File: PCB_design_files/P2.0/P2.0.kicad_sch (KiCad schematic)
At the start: 54 parts, among them J1 EEG_IN, J3 SWD, U1 INA819IDRGR, U3 TPS61094, U4 TPS60400, U5 NRF52832-QFAA-R, X1 32MHz

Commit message: P2.0
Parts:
- C1, C10, C11, C2, C7: footprint Capacitor_SMD:C_0805_2012Metric -> Capacitor_SMD:C_0402_1005Metric; Purchasing (none) -> https://www.digikey.ca/en/products/detail/murata-electronic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
- C12, C13, C14, C15, C16, C17, C18, L1: Purchasing (none) -> https://www.digikey.ca/en/products/detail/murata-electronic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
- C19, C20: footprint Capacitor_SMD:C_0603_1608Metric -> Capacitor_SMD:C_0402_1005Metric; Purchasing (none) -> https://www.digikey.ca/en/products/detail/murata-electronic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
- C3, C4, C5, C6: footprint Capacitor_SMD:C_0201_0603Metric -> Capacitor_SMD:C_0402_1005Metric; Purchasing (none) -> https://www.digikey.ca/en/products/detail/murata-electronic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
- C8: Field4 (none) -> https://www.digikey.ca/en/products/detail/murata-electronic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
- C9: Purchasing (none) -> https://www.digikey.ca/en/products/detail/tdk-corporation/C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
- L2, L3: footprint Inductor_SMD:L_0402_1005Metric -> Inductor_SMD:L_Murata_DFE201610P; Purchasing (none) -> https://www.digikey.ca/en/products/detail/murata-electronic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
- R1, R2: footprint Resistor_SMD:R_0402_1005Metric -> Resistor_SMD:R_0805_2012Metric; Purchasing (none) -> https://www.digikey.ca/en/products/detail/panasonic-electro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
- R10, R11, R12, R13, R14, R16, R17, R18, R19, R20, R4, R5, R7, R8, R9: footprint Resistor_SMD:R_0402_1005Metric -> Resistor_SMD:R_0805_2012Metric; Purchasing (none) -> https://www.digikey.ca/en/products/detail/stackpole-electro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
- R3: footprint Resistor_SMD:R_0402_1005Metric -> Resistor_SMD:R_0805_2012Metric; Puchasing (none) -> https://www.digikey.ca/en/products/detail/stackpole-electro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
- R6: value 100k -> 20k; footprint Resistor_SMD:R_0402_1005Metric -> Resistor_SMD:R_0805_2012Metric; Purchasing (none) -> https://www.digikey.ca/en/products/detail/stackpole-electro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
- U1: footprint Library:SON_9IDRGR_TEX -> Package_SON:WSON-8-1EP_3x3mm_P0.5mm_EP1.45x2.4mm_ThermalVias; Purchasing (none) -> https://www.digikey.ca/en/products/detail/texas-instruments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
- U2: footprint (none) -> Package_DFN_QFN:Texas_R-PUQFN-N10; Purchasing (none) -> https://www.digikey.com/en/products/detail/texas-instrument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
- U3: footprint Library:TPS61094DSSR -> Package_SON:WSON-12-1EP_3x2mm_P0.5mm_EP1x2.65_ThermalVias; Purchasing (none) -> https://www.digikey.ca/en/products/detail/texas-instruments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
- U4: footprint (none) -> Package_TO_SOT_SMD:SOT-23-5; Puchasing (none) -> https://www.digikey.com/en/products/detail/texas-instrument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
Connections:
- net +3V3: now also U4.2 (IN); no longer U4.1 (IN)
- net -3V3: now also U4.1 (OUT); no longer U4.5 (OUT)
- net GND: now also U4.4 (GND); no longer U4.2 (GND)
- net at C10.1: now also U4.5 (CFLY+); no longer U4.3 (CFLY+)
- net at C10.2: now also U4.3 (CFLY-); no longer U4.4 (CFLY-)
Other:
- moved on the sheet: C10

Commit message: Updated schematic
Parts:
- removed J3: SWD, symbol Connector:Conn_01x03_Pin
- removed X1: 32MHz, symbol Device:Crystal
- added J2: 20021121-00008C4LF, 20021121_00008C4LF:AMPHENOL_20021121-00008C4LF, symbol Connector_Generic:Conn_02x04_Counter_Clockwise
- added Y1: 32MHz, ECS_320_8_37CKM:XTAL_ECS-320-8-37CKM, symbol Device:Crystal_GND24
- AE1: Purchasing (none) -> https://www.digikey.ca/en/products/detail/johanson-technolo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
- BT1: footprint Connector_JST:JST_ACH_BM02B-ACHSS-GAN-ETF_1x02-1MP_P1.20mm_Vertical -> Connector_PinSocket_2.54mm:PinSocket_1x02_P2.54mm_Vertical; Purchasing (none) -> n/a
- J1: footprint Connector_JST:JST_SH_BM02B-SRSS-TB_1x02-1MP_P1.00mm_Vertical -> Connector_PinSocket_2.54mm:PinSocket_1x02_P2.54mm_Vertical; Purchasing (none) -> n/a
- U2: value ~ -> TLV9102
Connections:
- net +3V3: now also J2.2 (Pin_2)
- net GND: now also J2.3 (Pin_3), J2.4 (Pin_4), Y1.2, Y1.4
- net STAGE_3_OUT: now also J2.1 (Pin_1)
- net at C18.2, U5.34 (XC1): now also Y1.3
- net SWO: now reaches U5.21 (P0.18/TRACEDATA[0]/SWO)
- net SWO: now also J2.6 (Pin_6)
- net NRST: now reaches U5.24 (P0.21/Nreset)
- net NRST: now also J2.5 (Pin_5)
- net SWDCLK: now reaches U5.25 (SWDCLK)
- net SWDCLK: now also J2.7 (Pin_7)
- net SWDIO: now reaches U5.26 (SWDIO)
- net SWDIO: now also J2.8 (Pin_8)
- net at C16.2, U5.35 (XC2): now also Y1.1
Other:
- note added: "4. Debug Header"
- moved on the sheet: C13, C16, C17, C18, C21

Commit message: Updated LED footprint
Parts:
- D1: footprint LED_SMD:LED_0402_1005Metric -> LED_SMD:LED_0603_1608Metric; Purchasing (none) -> https://www.digikey.ca/en/products/detail/w%C3%BCrth-elektr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
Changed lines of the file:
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@@
       (effects (font (size 1.27 1.27)) (justify right))
     )
-    (property "Footprint" "LED_SMD:LED_0402_1005Metric" (at 199.39 143.51 0)
+    (property "Footprint" "LED_SMD:LED_0603_1608Metric" (at 199.39 143.51 0)
       (effects (font (size 1.27 1.27)) hide)
     )
-    (property "Datasheet" "~" (at 199.39 143.51 0)
+    (property "Datasheet" "https://www.we-online.com/components/products/datasheet/150060VS75000.pdf" (at 199.39 143.51 0)
       (effects (font (size 1.27 1.27)) hide)
     )
+    (property "Purchasing" "https://www.digikey.ca/en/products/detail/w%C3%BCrth-elektronik/150060VS75000/4489906" (at 199.39 143.51 90)
+      (effects (font (size 1.27 1.27)) hide)
+    )

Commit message: Added decoupling capacitors and updated layout
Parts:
- added C22, C23, C24, C25: .1uF, Capacitor_SMD:C_0402_1005Metric, symbol Device:C
- C21: value N.C. -> ~; now fitted; now left out of the parts list
- J1: footprint Connector_PinSocket_2.54mm:PinSocket_1x02_P2.54mm_Vertical -> Connector_PinHeader_2.54mm:PinHeader_1x02_P2.54mm_Vertical
- R18, R20: footprint Resistor_SMD:R_0805_2012Metric -> Resistor_SMD:R_0603_1608Metric; Purchasing https://www.digikey.ca/en/products/detail/stackpole-electro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 -> (none)
- U1: footprint Package_SON:WSON-8-1EP_3x3mm_P0.5mm_EP1.45x2.4mm_ThermalVias -> Package_SON:WSON-8-1EP_3x3mm_P0.5mm_EP1.45x2.4mm
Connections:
- net +3V3: now also C22.2, C24.1
- net -3V3: now also C23.2, C25.2
- net GND: now also C22.1, C23.1, C24.2, C25.1
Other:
- moved on the sheet: C2, C3, C4, C5, C6, C7, R10, R11, R12, R13, R14, R16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

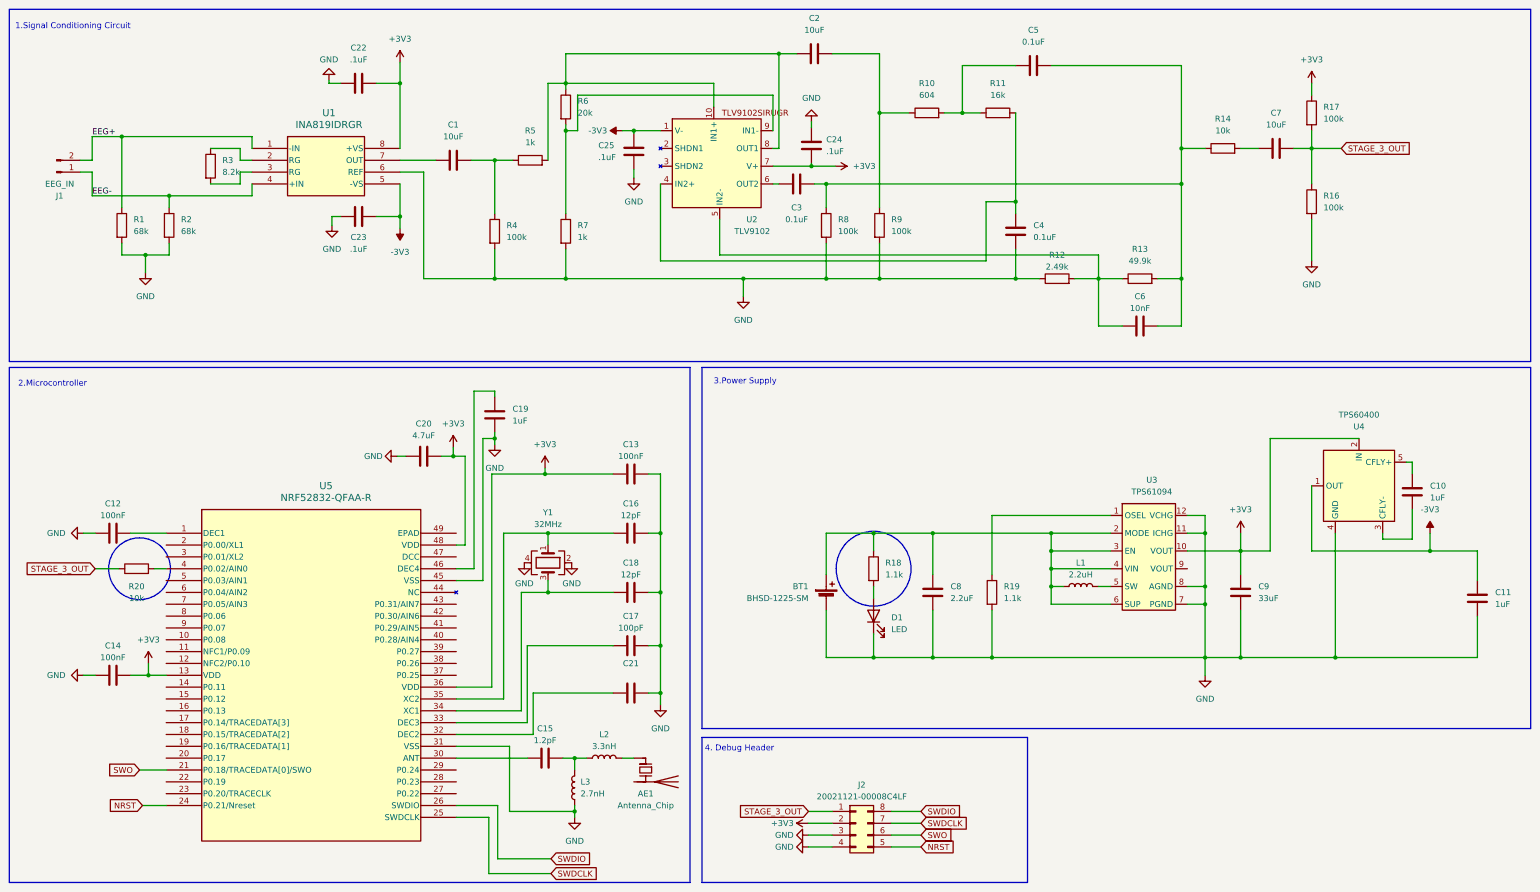
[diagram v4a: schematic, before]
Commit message: PCB layout updates
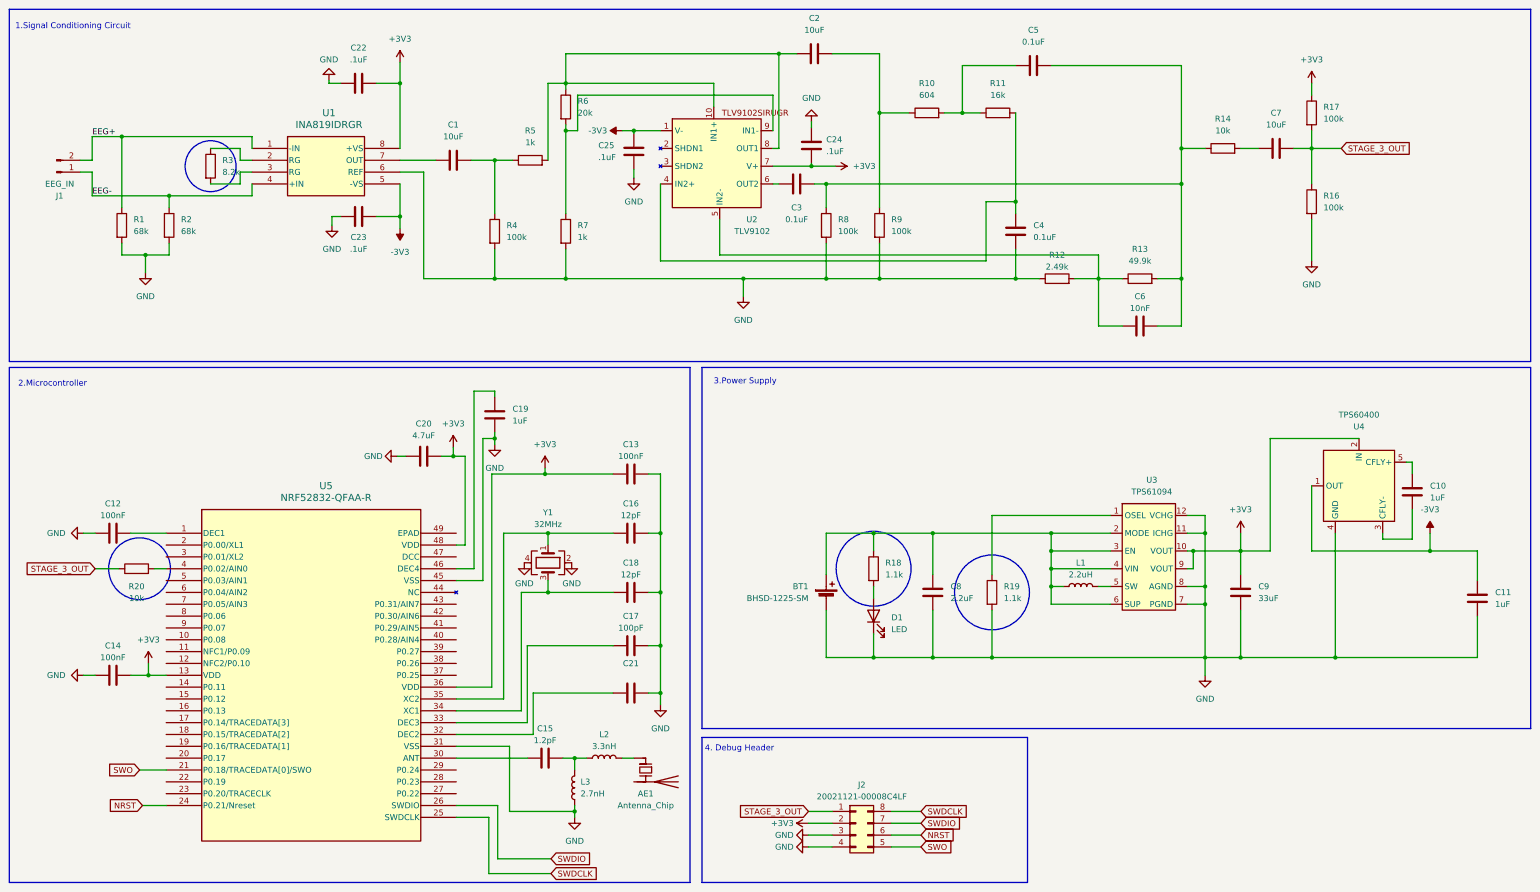
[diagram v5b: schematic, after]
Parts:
- R19: footprint Resistor_SMD:R_0805_2012Metric -> Resistor_SMD:R_0603_1608Metric; Purchasing https://www.digikey.ca/en/products/detail/stackpole-electro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 -> (none)
- R3: footprint Resistor_SMD:R_0805_2012Metric -> Resistor_SMD:R_0603_1608Metric
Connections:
- net +3V3: now also U3.9 (VOUT)
- net NRST: now also J2.6 (Pin_6); no longer J2.5 (Pin_5)
- net SWDCLK: now also J2.8 (Pin_8); no longer J2.7 (Pin_7)
- net SWDIO: now also J2.7 (Pin_7); no longer J2.8 (Pin_8)
- net SWO: now also J2.5 (Pin_5); no longer J2.6 (Pin_6)
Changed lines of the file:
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@@
   (junction (at 118.11 45.72) (diameter 0) (color 0 0 0 0)
   )
+  (junction (at 267.97 129.54) (diameter 0) (color 0 0 0 0)
+  )
   (junction (at 278.13 129.54) (diameter 0) (color 0 0 0 0)
   )
@@
   (junction (at 153.67 149.86) (diameter 0) (color 0 0 0 0)
   )
+  (wire (pts (xy 267.97 129.54) (xy 278.13 129.54))
+    (stroke (width 0) (type default))
+  )
   (wire (pts (xy 102.87 48.26) (xy 102.87 71.12))
     (stroke (width 0) (type default))
@@
     (stroke (width 0) (type default))
   )
+  (wire (pts (xy 266.7 133.35) (xy 267.97 133.35))
+    (stroke (width 0) (type default))
+  )
   (wire (pts (xy 189.23 50.8) (xy 265.43 50.8))
     (stroke (width 0) (type default))
@@
     (stroke (width 0) (type default))
   )
+  (wire (pts (xy 267.97 133.35) (xy 267.97 129.54))
+    (stroke (width 0) (type default))
+  )
   (wire (pts (xy 118.11 64.77) (xy 118.11 71.12))
     (stroke (width 0) (type default))
@@
     (stroke (width 0) (type default))
   )
-  (wire (pts (xy 266.7 129.54) (xy 278.13 129.54))
+  (wire (pts (xy 266.7 129.54) (xy 267.97 129.54))
     (stroke (width 0) (type default))
   )
@@
     (fill (type none))
   )
+  (circle (center 224.79 138.43) (radius 8.0322)
+    (stroke (width 0) (type default))
+    (fill (type none))
+  )
   (rectangle (start 162.56 90.17) (end 340.36 167.64)
+    (stroke (width 0) (type default))
+    (fill (type none))
+  )
+  (circle (center 57.15 46.99) (radius 5.4625)
     (stroke (width 0) (type default))
     (fill (type none))
@@
     )
   )
-  (global_label "NRST" (shape input) (at 209.55 193.04 0) (fields_autoplaced)
+  (global_label "SWO" (shape input) (at 209.55 193.04 0) (fields_autoplaced)
     (effects (font (size 1.27 1.27)) (justify left))
-    (property "Intersheetrefs" "${INTERSHEET_REFS}" (at 217.3128 193.04 0)
+    (property "Intersheetrefs" "${INTERSHEET_REFS}" (at 216.5266 193.04 0)
       (effects (font (size 1.27 1.27)) (justify left) hide)
     )
@@
     )
   )
-  (global_label "SWO" (shape input) (at 209.55 190.5 0) (fields_autoplaced)
+  (global_label "NRST" (shape input) (at 209.55 190.5 0) (fields_autoplaced)
     (effects (font (size 1.27 1.27)) (justify left))
-    (property "Intersheetrefs" "${INTERSHEET_REFS}" (at 216.5266 190.5 0)
+    (property "Intersheetrefs" "${INTERSHEET_REFS}" (at 217.3128 190.5 0)
       (effects (font (size 1.27 1.27)) (justify left) hide)
     )
@@
     )
   )
-  (global_label "SWDCLK" (shape input) (at 209.55 187.96 0) (fields_autoplaced)
+  (global_label "SWDIO" (shape input) (at 209.55 187.96 0) (fields_autoplaced)
     (effects (font (size 1.27 1.27)) (justify left))
-    (property "Intersheetrefs" "${INTERSHEET_REFS}" (at 220.0342 187.96 0)
+    (property "Intersheetrefs" "${INTERSHEET_REFS}" (at 218.4014 187.96 0)
       (effects (font (size 1.27 1.27)) (justify left) hide)
     )
   )
-  (global_label "SWDIO" (shape input) (at 209.55 185.42 0) (fields_autoplaced)
+  (global_label "SWDCLK" (shape input) (at 209.55 185.42 0) (fields_autoplaced)
     (effects (font (size 1.27 1.27)) (justify left))
-    (property "Intersheetrefs" "${INTERSHEET_REFS}" (at 218.4014 185.42 0)
+    (property "Intersheetrefs" "${INTERSHEET_REFS}" (at 220.0342 185.42 0)
       (effects (font (size 1.27 1.27)) (justify left) hide)
     )
@@
       (effects (font (size 1.27 1.27)) (justify left))
     )
-    (property "Footprint" "Resistor_SMD:R_0805_2012Metric" (at 55.372 46.99 90)
+    (property "Footprint" "Resistor_SMD:R_0603_1608Metric" (at 55.372 46.99 90)
       (effects (font (size 1.27 1.27)) hide)
     )
@@
       (effects (font (size 1.27 1.27)) (justify left))
     )
-    (property "Footprint" "Resistor_SMD:R_0805_2012Metric" (at 223.012 138.43 90)
-      (effects (font (size 1.27 1.27)) hide)
-    )
-    (property "Datasheet" "https://www.seielect.com/catalog/sei-rmcf_rmcp.pdf" (at 224.79 138.43 0)
-      (effects (font (size 1.27 1.27)) hide)
-    )
-    (property "Purchasing" "https://www.digikey.ca/en/products/detail/stackpole-electronics-inc/RMCF0805FG1K10/1760461" (at 224.79 138.43 0)
-      (effects (font (size 1.27 1.27)) hide)
-    )
+    (property "Footprint" "Resistor_SMD:R_0603_1608Metric" (at 223.012 138.43 90)
+      (effects (font (size 1.27 1.27)) hide)
+    )
+    (property "Datasheet" "" (at 224.79 138.43 0)
+      (effects (font (size 1.27 1.27)) hide)
+    )
+    (property "Purchasing" "" (at 224.79 138.43 0)
+      (effects (font (size 1.27 1.27)) hide)
+    )

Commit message: Changed all resistor footprints to 0402
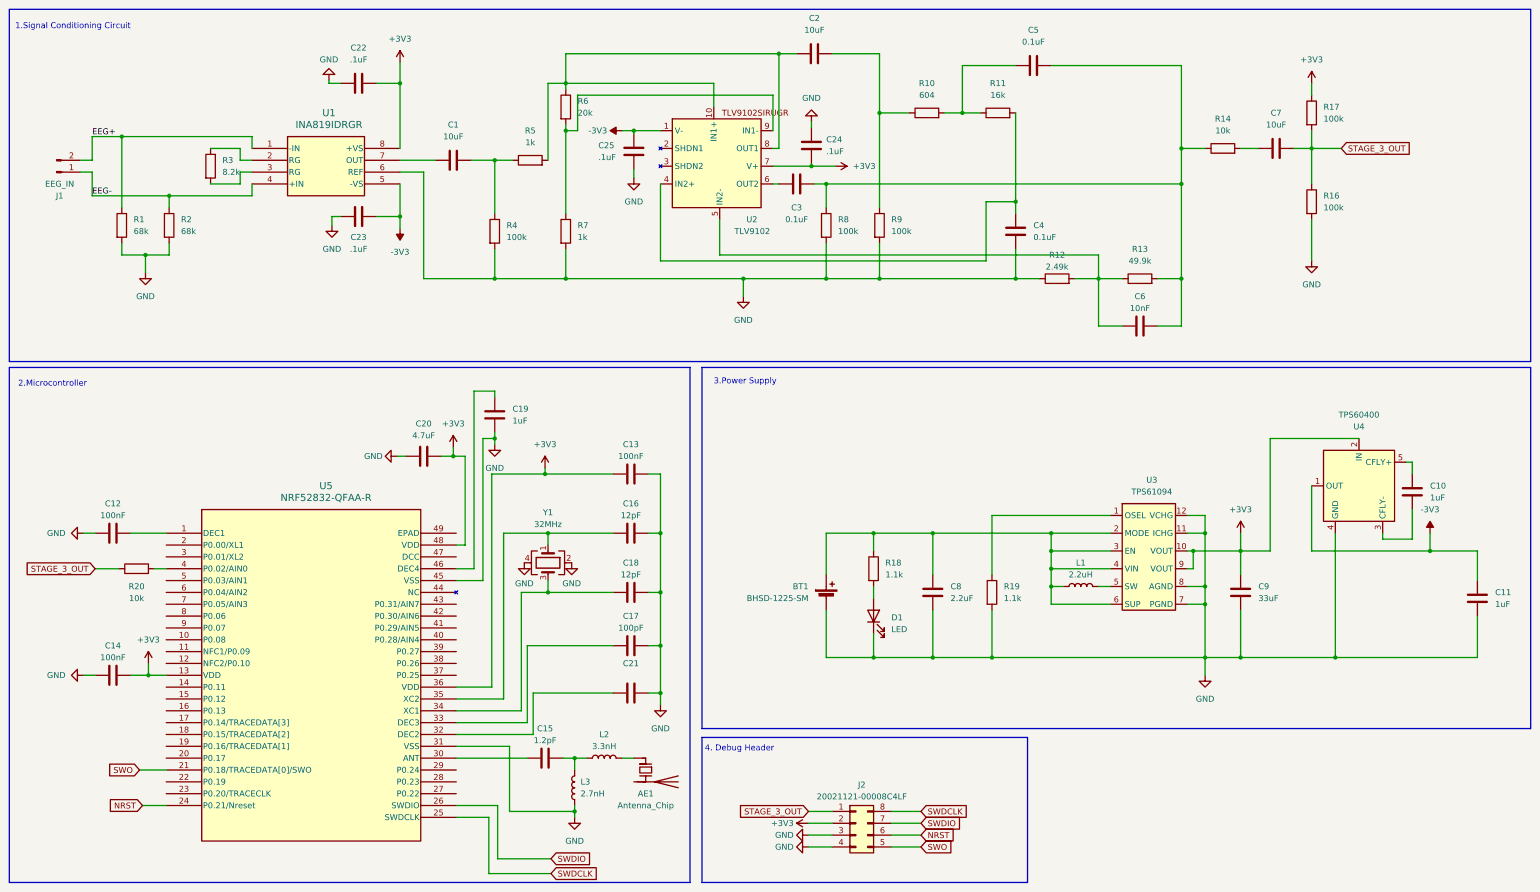
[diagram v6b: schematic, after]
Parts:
- R1, R2: footprint Resistor_SMD:R_0805_2012Metric -> Resistor_SMD:R_0402_1005Metric; Purchasing https://www.digikey.ca/en/products/detail/panasonic-electro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 -> (none)
- R10, R11, R12, R13, R14, R16, R17, R4, R5, R6, R7, R8, R9: footprint Resistor_SMD:R_0805_2012Metric -> Resistor_SMD:R_0402_1005Metric; Purchasing https://www.digikey.ca/en/products/detail/stackpole-electro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 -> (none)
- R18, R19, R20: footprint Resistor_SMD:R_0603_1608Metric -> Resistor_SMD:R_0402_1005Metric
- R3: footprint Resistor_SMD:R_0603_1608Metric -> Resistor_SMD:R_0402_1005Metric; Puchasing https://www.digikey.ca/en/products/detail/stackpole-electro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 -> (none)
- U3: footprint Package_SON:WSON-12-1EP_3x2mm_P0.5mm_EP1x2.65_ThermalVias -> Package_SON:WSON-12-1EP_3x2mm_P0.5mm_EP1x2.65
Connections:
- net at C3.2, C6.2, R13.2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: now also C5.2; no longer C5.1
- net at R10.2, R11.1: now also C5.1; no longer C5.2
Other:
- moved on the sheet: C5

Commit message: Changed manufacturing and descirptions of passive comoponents
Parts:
- AE1: Purchasing https://www.digikey.ca/en/products/detail/johanson-technolo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 -> (none)
- BT1, J1: Purchasing n/a -> (none)
- C1, C10, C11, C12, C13, C14, C15, C16, C17, C18, C19, C2, C20, C22, C23, C24, C25, C3, C4, C5, C6, C7, L1, L2, L3: Purchasing https://www.digikey.ca/en/products/detail/murata-electronic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 -> (none)
- C8: Field4 https://www.digikey.ca/en/products/detail/murata-electronic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 -> (none)
- C9: Purchasing https://www.digikey.ca/en/products/detail/tdk-corporation/C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 -> (none)
- D1: Purchasing https://www.digikey.ca/en/products/detail/w%C3%BCrth-elektr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 -> (none)
- J2: Purchasing https://www.digikey.ca/en/products/detail/amphenol-cs-fci/2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 -> (none)
- R1, R2: Manufacturer (none) -> Stackpole Electronics Inc; Part Number (none) -> RMCF0402FT68K0
- R10: Manufacturer (none) -> Stackpole Electronics Inc; Part Number (none) -> RMCF0402FT604R
- R11: Manufacturer (none) -> Stackpole Electronics Inc; Part Number (none) -> RMCF0402FT16K0
- R12: Manufacturer (none) -> Stackpole Electronics Inc; Part Number (none) -> RMCF0402FT2K49
- R13: Manufacturer (none) -> Stackpole Electronics Inc; Part Number (none) -> RMCF0402FT49K9
- R14, R20: Manufacturer (none) -> Stackpole Electronics Inc; Part Number (none) -> RMCF0402FT10K0
- R16, R17, R4, R8, R9: Manufacturer (none) -> Stackpole Electronics Inc; Part Number (none) -> RMCF0402FT100K
- R18, R19: Manufacturer (none) -> Stackpole Electronics Inc; Part Number (none) -> RMCF0402FT1K10
- R3: Manufacturer (none) -> Stackpole Electronics Inc; Part Number (none) -> RMCF0402FT8K20
- R5, R7: Manufacturer (none) -> Stackpole Electronics Inc; Part Number (none) -> RMCF0402FT1K00
- R6: Manufacturer (none) -> Stackpole Electronics Inc; Part Number (none) -> RMCF0402FT20K0
- U1: Manufacturer (none) -> Texas Instruments; Part Number (none) -> INA819IDRGR; Purchasing https://www.digikey.ca/en/products/detail/texas-instruments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 -> (none)
- U2: Manufacturer (none) -> Texas Instruments; Part Number (none) -> TLV9102SIRUGR; Purchasing https://www.digikey.com/en/products/detail/texas-instrument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 -> (none)
- U3: Manufacturer (none) -> Texas Instruments; Part Number (none) -> TPS61094; Purchasing https://www.digikey.ca/en/products/detail/texas-instruments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 -> (none)
- U4: Manufacturer (none) -> Texas Instruments; Part Number (none) -> TPS60400DBV; Puchasing https://www.digikey.com/en/products/detail/texas-instrument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 -> (none)
- Y1: Purchasing https://www.digikey.ca/en/products/detail/ecs-inc/ECS-320-8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 -> (none)
